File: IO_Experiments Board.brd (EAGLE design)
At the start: 230 x 200 mm, 191 parts, among them IC1 ULN2803, IC10 ULN2803, IC11 NX1117CE33Z, IC13 L298, IC2 4511N, IC3 PCF8563P, IC4 MCP23017SP, IC5 MAX7219CNG, IC6 74125N, IC7 AT24CP, IC8 MCP23017SP, IC9 MCP23017SP, K1 G2RA, K2 G2RA, K3 G2RA, K4 G2RA, K5 G2RA, K6 G2RA, K7 G2RA, K8 G2RA, Q1 32.768 kHz, SW1 EC12E_SW, T1 BC547, T2 BC547, T3 BC547, T4 BC547, U2 JOYSTICK, X2 POWERSUPPLY_DC21MMX

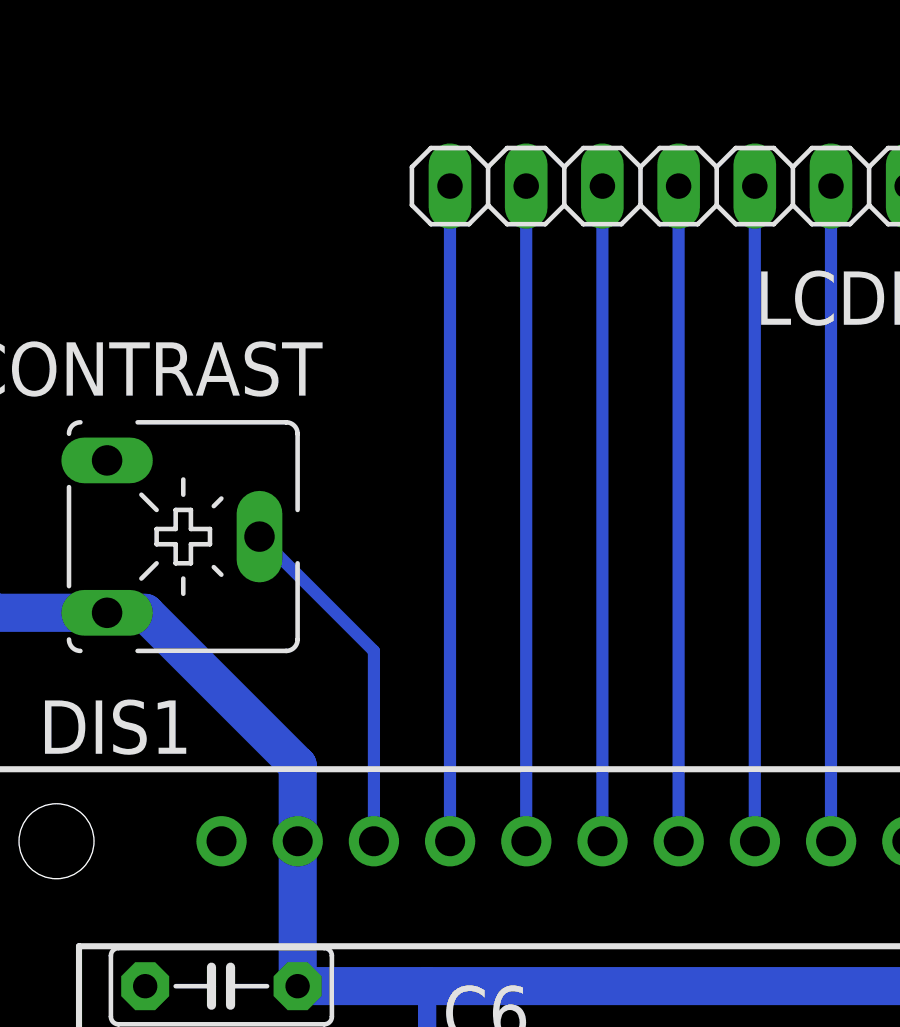
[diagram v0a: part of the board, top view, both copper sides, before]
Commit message: added signal names on connectors on the board , layer 51
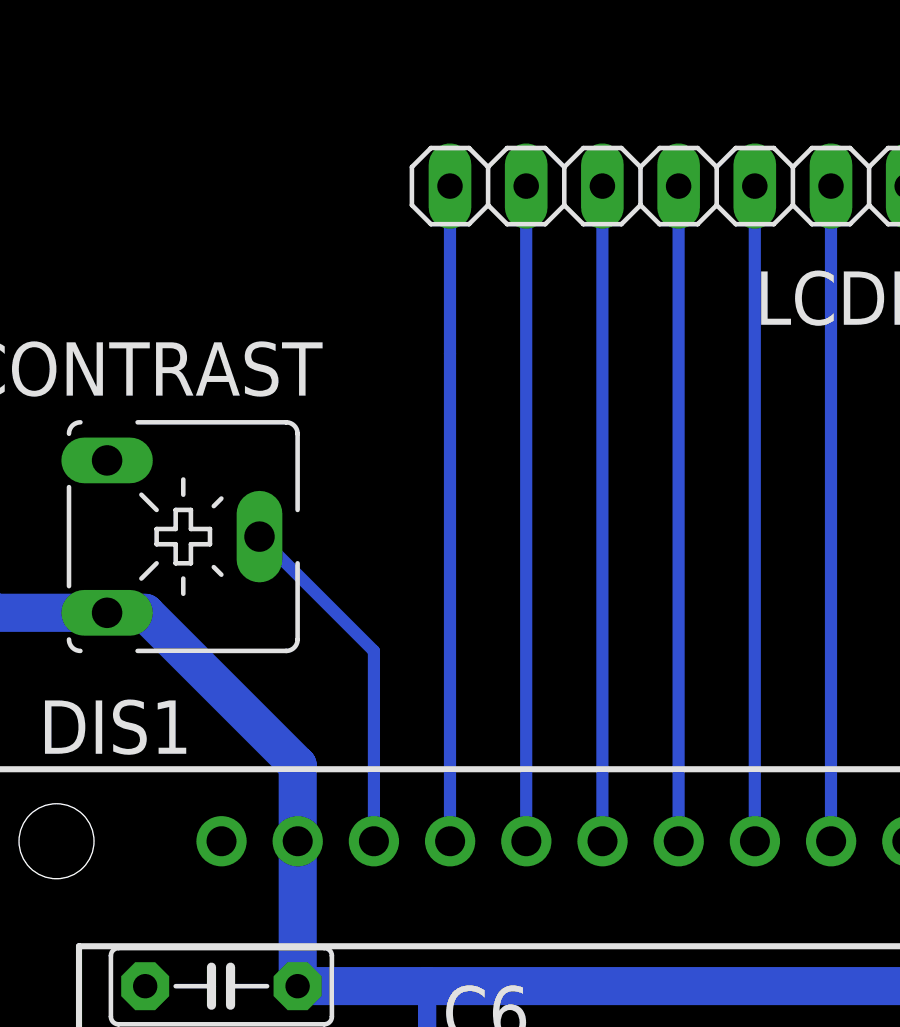
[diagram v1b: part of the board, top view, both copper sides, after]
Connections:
- net N$116 renamed REL1
- net N$120 renamed REL2
- net N$121 renamed REL3
- net N$122 renamed 2A0
- net N$123 renamed 2A1
- net N$124 renamed 2A2
- net N$125 renamed 2A3
- net N$126 renamed 2A4
- net N$127 renamed 2A5
- net N$128 renamed 2A6
- net N$129 renamed 2A7
- net N$130 renamed 2B0
- net N$131 renamed 2B1
- net N$132 renamed 2B2
- net N$133 renamed 2B3
- net N$134 renamed 2B4
- net N$135 renamed 2B5
- net N$136 renamed 2B6
- net N$137 renamed 2B7
- net N$141 renamed 3A0
- net N$142 renamed 3A1
- net N$143 renamed 3A2
- net N$144 renamed 3A3
- net N$145 renamed 3A4
- net N$146 renamed 3A5
- net N$147 renamed 3A6
- net N$148 renamed 3A7
- net N$149 renamed 3B0
- net N$150 renamed 3B1
- net N$151 renamed 3B2
- net N$152 renamed 3B3
- net N$153 renamed 3B4
- net N$154 renamed 3B5
- net N$155 renamed 3B6
- net N$156 renamed 3B7
- net N$160 renamed REL4
- net N$161 renamed REL5
- net N$162 renamed REL6
- net N$163 renamed REL7
- net N$164 renamed REL8
- net N$25 renamed CONTRAST
- net N$27 renamed LCD_E
- net N$35 renamed LCD_RW
- net N$36 renamed LCD_RS
- net N$37 renamed LCD_D0
- net N$38 renamed LCD_D1
- net N$39 renamed LCD_D2
- net N$40 renamed LCD_D3
- net N$41 renamed LCD_D4
- net N$42 renamed LCD_D5
- net N$43 renamed LCD_D6
- net N$44 renamed LCD_D7
- net N$60 renamed IA
- net N$61 renamed IB
- net N$62 renamed IC
- net N$63 renamed ID
- net N$64 renamed D1
- net N$65 renamed D2
- net N$66 renamed D3
- net N$67 renamed D4
- net N$68 renamed 1A0
- net N$69 renamed 1A1
- net N$70 renamed 1A2
- net N$71 renamed 1A3
- net N$72 renamed 1A4
- net N$75 renamed 1A5
- net N$76 renamed 1A6
- net N$77 renamed 1A7
- net N$78 renamed 1B0
- net N$79 renamed 1B1
- net N$80 renamed 1B2
- net N$81 renamed 1B3
- net N$82 renamed 1B4
- net N$83 renamed 1B5
- net N$84 renamed 1B6
- net N$85 renamed 1B7
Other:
- board text added: "+5V"
- board text added: "+5V_OUT"
- board text added: "0"
- board text added: "1"
- board text added: "2"
- board text added: "3"
- board text added: "4"
- board text added: "4 x 7SEG"
- board text added: "5"
- board text added: "6"
- board text added: "7"
- board text added: "8"
- board text added: "A"
- board text added: "ADC_CS"
- board text added: "ADC_IN"
- board text added: "ANT"
- board text added: "AUREL RF MODULE"
- board text added: "B"
- board text added: "BUTTONS"
- board text added: "BUZZER"
- board text added: "D0"
- board text added: "D1"
- board text added: "D2"
- board text added: "D3"
- board text added: "D4"
- board text added: "D5"
- board text added: "D6"
- board text added: "D7"
- board text added: "DAC_CS"
- board text added: "DAC_OUT"
- board text added: "DIRA"
- board text added: "DIRA#"
- board text added: "DIRB"
- board text added: "DIRB#"
- board text added: "E"
- board text added: "ENABLE"
- board text added: "ENCODER_A"
- board text added: "ENCODER_B"
- board text added: "ENCODER_SWITCH"
- board text added: "EXT1"
- board text added: "EXT2"
- board text added: "EXT3"
- board text added: "EXT_SENS1"
- board text added: "EXT_SENS2"
- board text added: "EXT_SENS3"
- board text added: "FLASH_CS"
- board text added: "GND"
- board text added: "I2C ADDRESS"
- board text added: "I2C_SCL"
- board text added: "I2C_SDA"
- board text added: "IB"
- board text added: "IC"
- board text added: "ID"
- board text added: "IO-EXPANDER"
- board text added: "JOYSTICK_SWITCH"
- board text added: "JOYSTICK_VERTICAL"
- board text added: "JOYSTIC_HORIZONTAL"
- board text added: "LCD"
- board text added: "LCD CONTRAST"
- board text added: "LEDs"
- board text added: "MATRIX_DISPLAY_SS"
- board text added: "MOTOR DRIVE"
- board text added: "OUT1"
- board text added: "OUT2"
- board text added: "OUT3"
- board text added: "OUT4"
- board text added: "POTS"
- board text added: "PWMA"
- board text added: "PWMB"
- board text added: "REL1"
- board text added: "REL2"
- board text added: "REL3"
- board text added: "REL4"
- board text added: "REL5"
- board text added: "REL6"
- board text added: "REL7"
- board text added: "REL8"
- board text added: "RELAYs"
- board text added: "RS"
- board text added: "RW"
- board text added: "RX"
- board text added: "SENSOR_IR"
- board text added: "SENSOR_LIGHT"
- board text added: "SENSOR_TEMPERATURE"
- board text added: "SPI-MISO"
- board text added: "SPI-MOSI"
- board text added: "SPI_SCK"
- board text added: "SWITCHES"
- board text added: "TX"
- board text added: "TX/RX"
- board text added: "VIN"
